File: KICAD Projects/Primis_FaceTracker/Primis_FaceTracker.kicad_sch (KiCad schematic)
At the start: 48 parts, among them CN2 KH-FG0.5-H2.0-24PIN, J1 USB_C_Receptacle_USB2.0_16P, Q1 PMOS, SW1 SW_SPST, SW2 SW_SPST, U1 ESP32-S3-WROOM-1, U2 AMS1117-3.3, U3 XC6206P122MR, U5 XC6206P282MR

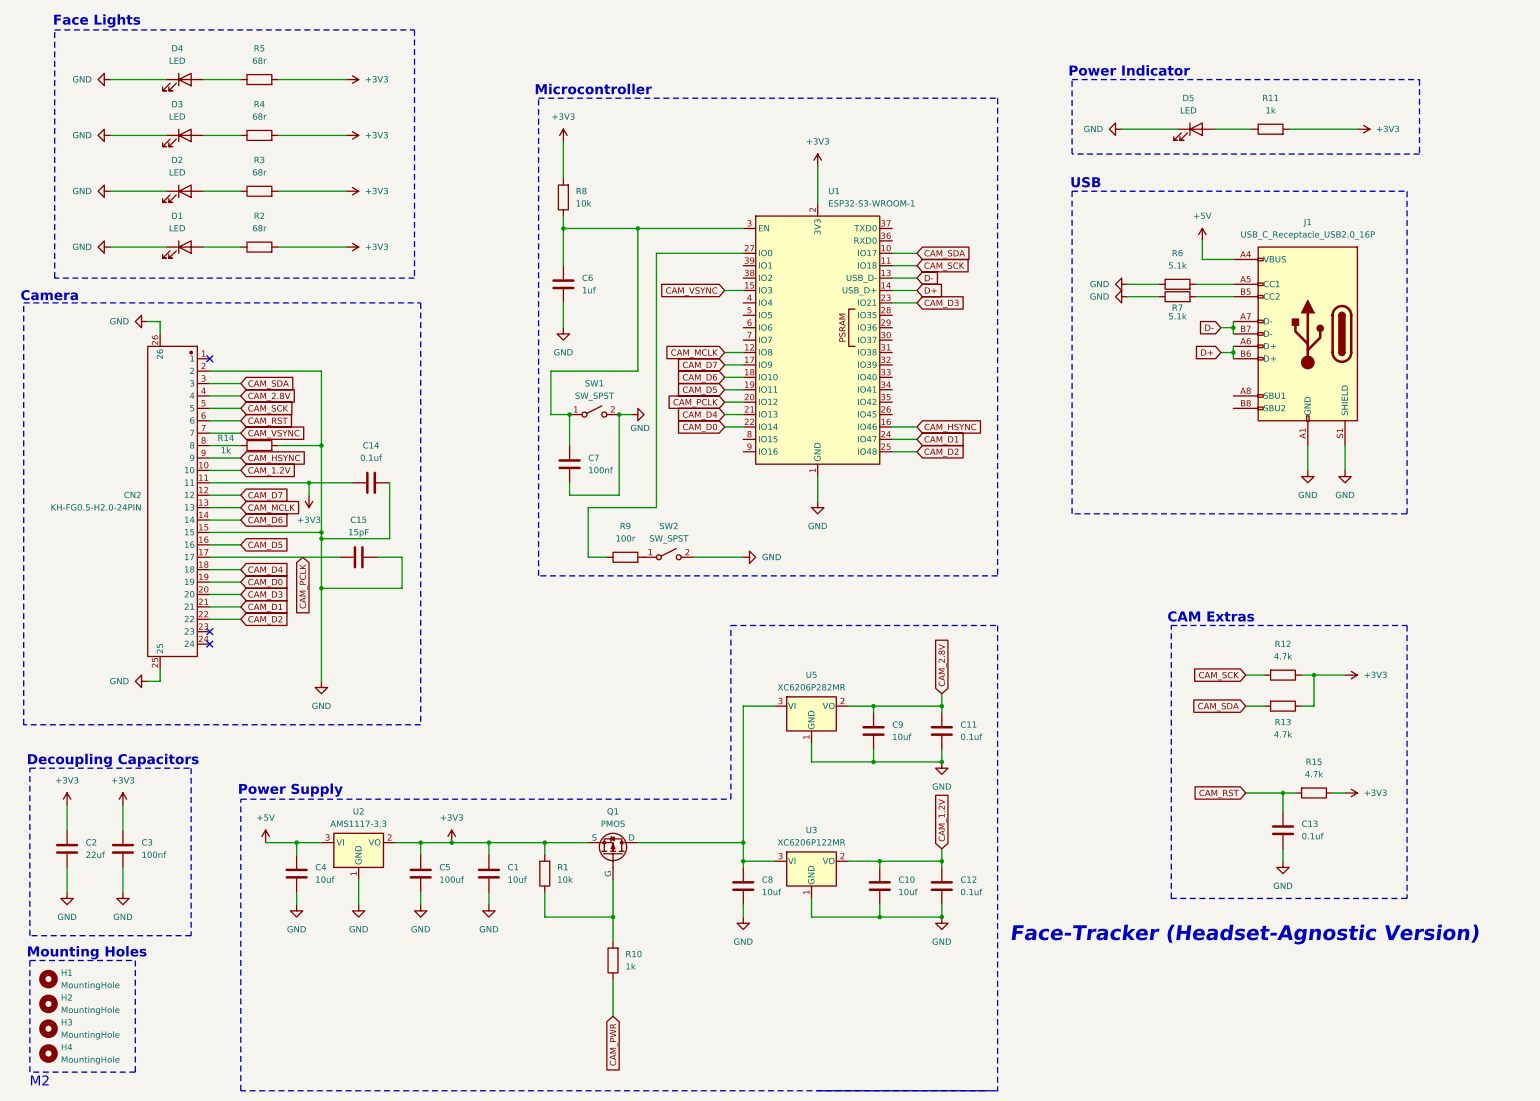
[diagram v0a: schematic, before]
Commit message: Gerbers plus clean up
-Added gerbers for the face tracker and versipellis
-Shrunk the face tracker and cleaned up
-Fixed some DRC issues with both projects
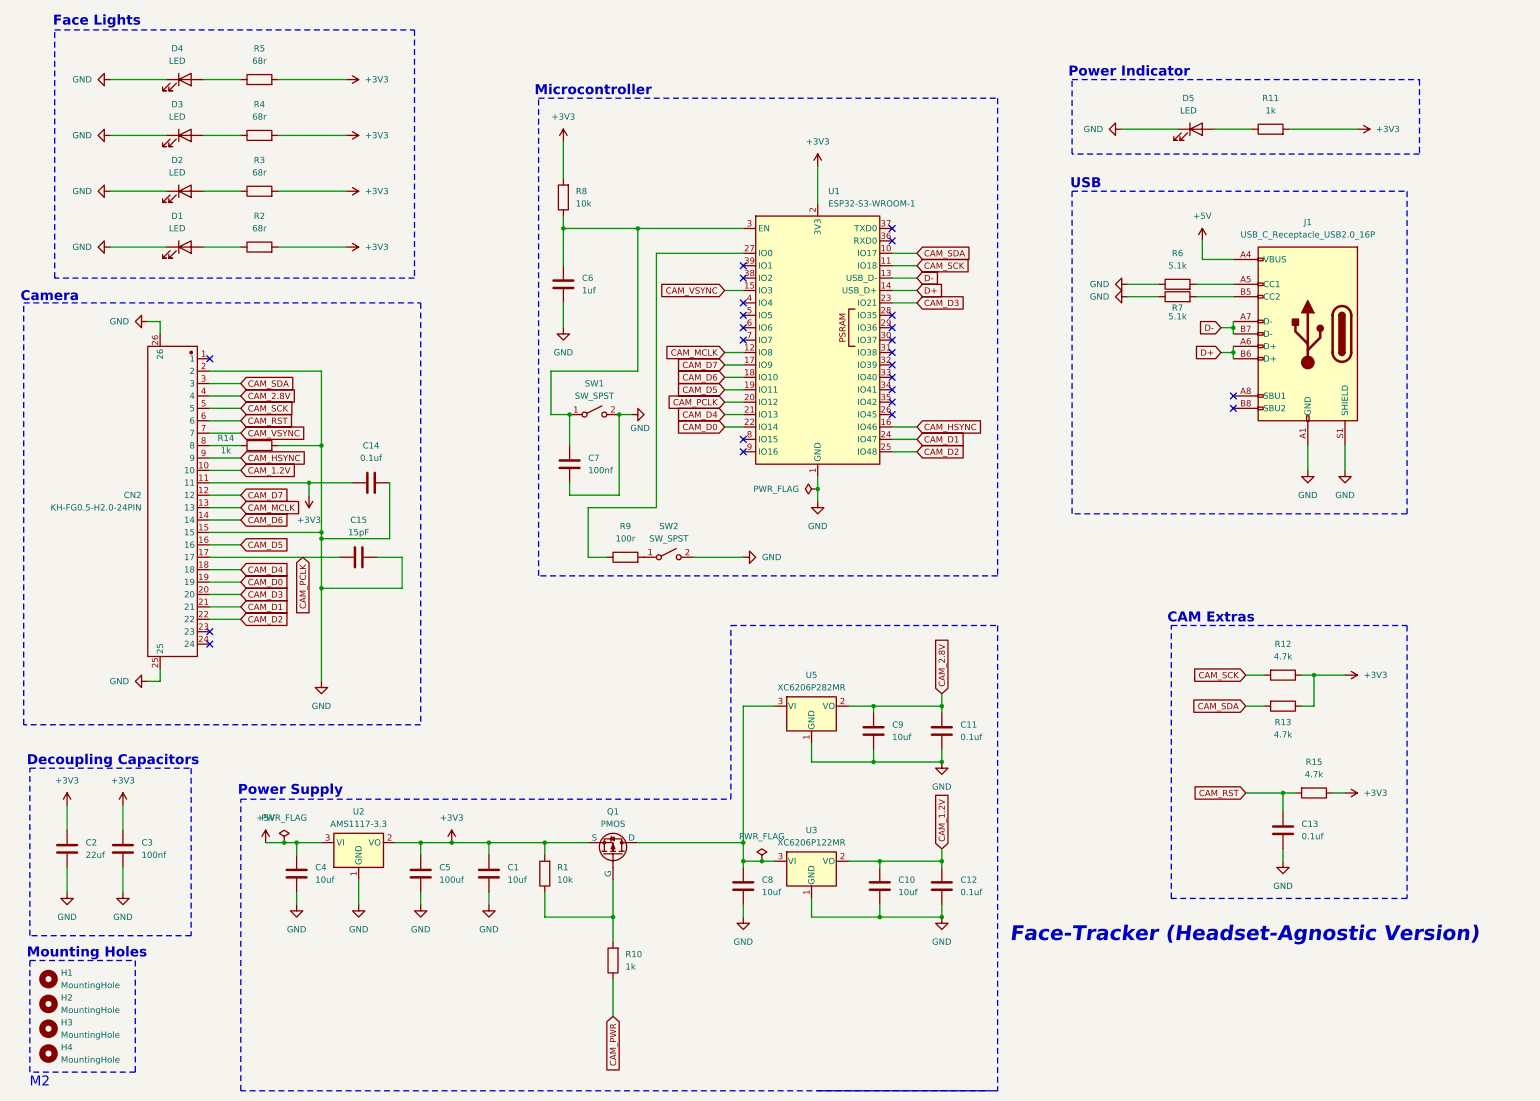
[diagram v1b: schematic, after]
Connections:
- no-connect marks 3 -> 24

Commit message: FaceTracker fixes and Dongle rework
-Fixed some mistakes on the Facetracker with the camera power lines.
-Some part swaps and additions on the dongle to match the JLCPCBs catalogue
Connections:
- net CAM_PWR: now also U1.9 (IO16)
- no-connect marks 24 -> 23
